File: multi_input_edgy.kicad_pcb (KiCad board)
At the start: 2 copper layers, 60 x 43.2 mm, 84 parts, among them J1 002, J2 002, J3 In1, J4 In2, J5 In3, J6 In4, J7 6V-24V, Q1 PMV213SN, Q10 DMP610DL, Q11 2N7002, Q12 2N7002, Q13 PMV213SN, Q14 DMP610DL, Q15 2N7002, Q16 2N7002, Q2 DMP610DL, Q3 2N7002, Q4 2N7002, Q5 PMV213SN, Q6 DMP610DL, Q7 2N7002, Q8 2N7002, Q9 PMV213SN, U1 EL3H7, U10 AL5809-15P, U11 EL3H7, U12 EL3H7, U13 AL5809-15P, U14 AL5809-15P, U15 EL3H7, U16 EL3H7, U17 HEF4021BT, U18 SN74LVC1G125, U2 AL5809-15P, U3 AL5809-15P, U4 EL3H7, U5 AL5809-15P, U6 AL5809-15P, U7 EL3H7, U8 EL3H7, U9 AL5809-15P

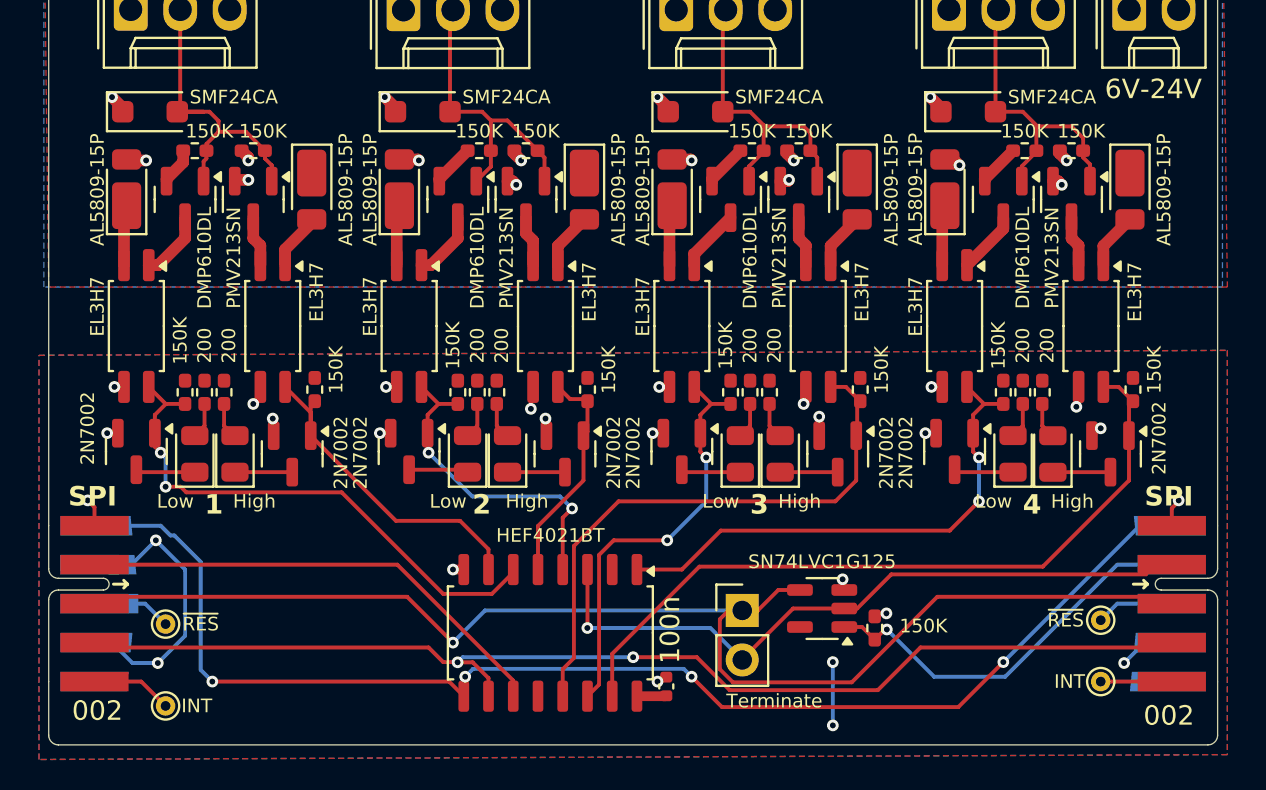
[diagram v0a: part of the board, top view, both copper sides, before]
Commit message: Fix constant current source (AL5809) symbol and footprint
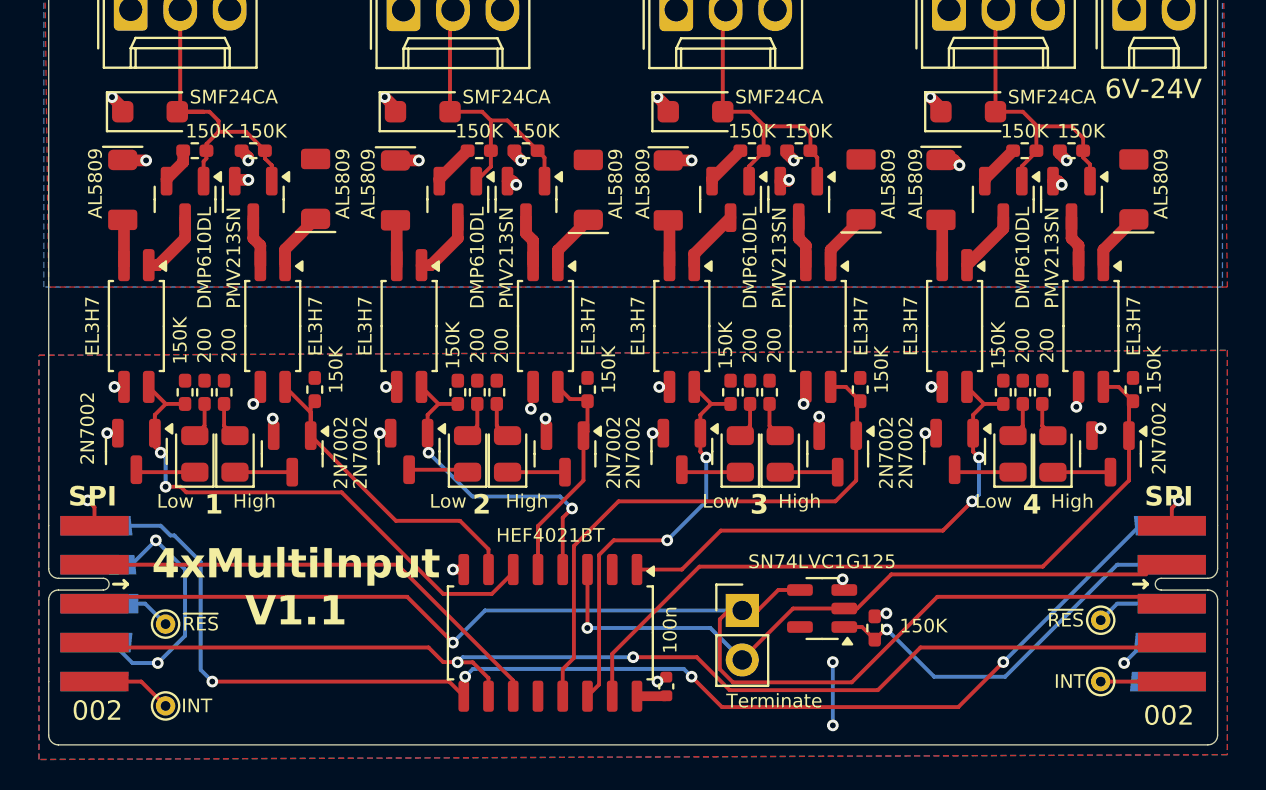
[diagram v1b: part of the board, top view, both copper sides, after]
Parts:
- U1, U11, U12, U15, U16, U4, U7, U8: footprint Package_SO:SSOP-4_4.4x2.6mm_P1.27mm -> lcsc_stuff:SSOP-4_4.4x2.6mm_P1.27mm
- U10, U13, U14, U2, U3, U5, U6, U9: value AL5809-15P -> AL5809; footprint Diode_SMD:D_PowerDI-123 -> lcsc_stuff:PowerDI-123
- moved U9 37.6 mm to (136.9, 50.4), turned to 90 degrees
- moved U6 37.6 mm to (188.6, 48.6), turned to -90 degrees
- moved U13 23.6 mm to (164.9, 50.4), turned to 90 degrees
- moved U3 23.6 mm to (160.6, 48.6), turned to -90 degrees
- moved U10 14.1 mm to (150.9, 50.4)
- moved U5 14.1 mm to (174.6, 48.6)
- moved U14 0.93 mm to (178.9, 50.4)
- moved U2 0.93 mm to (146.6, 48.6)
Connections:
- U10 pad 1: Net-(U10-VA) -> Net-(U10-in)
- U12 pad 2: Net-(U10-VA) -> Net-(U12-K)
- U13 pad 1: VDDA -> Net-(U12-K)
- U13 pad 2: Net-(U13-VB) -> GNDA
- U15 pad 1: Net-(U13-VB) -> Net-(U15-A)
- U3 pad 1: Net-(U3-VA) -> VDDA
- U3 pad 2: GNDA -> Net-(U3-Out)
- U4 pad 2: Net-(U3-VA) -> Net-(U4-K)
- U5 pad 2: Net-(U5-VB) -> Net-(U11-A)
- U6 pad 1: Net-(U6-VA) -> VDDA
- U6 pad 2: GNDA -> Net-(U15-A)
- U7 pad 1: Net-(U5-VB) -> Net-(U3-Out)
- U8 pad 2: Net-(U6-VA) -> Net-(U10-in)
- U9 pad 1: VDDA -> Net-(U4-K)
- U9 pad 2: Net-(U11-A) -> GNDA
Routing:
- net Net-(U6-VA): track 3.11 -> 0.00 mm
- net Net-(U3-VA): track 3.11 -> 0.00 mm
- net Net-(U10-VA): track 3.11 -> 0.00 mm
- net Net-(U15-A): track 0.00 -> 3.00 mm
- net Net-(U3-Out): track 0.00 -> 2.97 mm
- net Net-(U5-VB): track 2.92 -> 0.00 mm
- net Net-(U13-VB): track 2.92 -> 0.00 mm
- net Net-(U4-K): track 0.00 -> 2.35 mm
- net Net-(U10-in): track 0.00 -> 2.33 mm
- net Net-(U12-K): track 0.00 -> 2.31 mm
- net GNDA: track 12.8 -> 13.8 mm
- net Net-(U14-in): track 3.11 -> 2.35 mm
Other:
- board text added: "4xMultiInput V1.1"

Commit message: Get board name and version from text variable
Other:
- board text added: "${BoardName} ${Version}"
- board text removed: "4xMultiInput V1.1"
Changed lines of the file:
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@@
 		)
 	)
+	(property "BoardName" "4xMultiInput")
+	(property "Version" "V1.1")
 	(net 0 "")
 	(net 1 "GNDA")
@@
 	(net 15 "Net-(D9-K)")
 	(net 16 "Net-(D9-A)")
-	(net 17 "Net-(D11-A)")
-	(net 18 "Net-(D11-K)")
-	(net 19 "Net-(D12-A)")
-	(net 20 "Net-(D12-K)")
+	(net 17 "Net-(U14-in)")
+	(net 18 "Net-(U15-A)")
+	(net 19 "Net-(Q14-D)")
+	(net 20 "Net-(Q13-D)")
 	(net 21 "/4xInput/~{CS}")
 	(net 22 "/4xInput/MOSI")
@@
 	(net 27 "Net-(Q9-D)")
 	(net 28 "Net-(Q10-D)")
-	(net 29 "Net-(Q13-D)")
-	(net 30 "Net-(Q14-D)")
+	(net 29 "Net-(D12-K)")
+	(net 30 "Net-(D12-A)")
 	(net 31 "Net-(Q2-D)")
 	(net 32 "Net-(U1-A)")
@@
 	(net 34 "Net-(U11-A)")
 	(net 35 "Net-(U12-K)")
-	(net 36 "Net-(U15-A)")
+	(net 36 "Net-(D11-K)")
 	(net 37 "unconnected-(U17-Q6-Pad12)")
 	(net 38 "unconnected-(U17-Q5-Pad2)")
@@
 	(net 60 "Net-(U3-Out)")
 	(net 61 "Net-(U10-in)")
-	(net 62 "Net-(U14-in)")
+	(net 62 "Net-(D11-A)")
 	(footprint "Diode_SMD:D_SOD-123F"
 		(layer "F.Cu")
@@
 			(layers "F.Cu" "F.Mask" "F.Paste")
 			(roundrect_rratio 0.25)
-			(net 20 "Net-(D12-K)")
+			(net 29 "Net-(D12-K)")
 			(pinfunction "D")
 			(pintype "passive")
@@
 			(layers "F.Cu" "F.Mask" "F.Paste")
 			(roundrect_rratio 0.25)
-			(net 29 "Net-(Q13-D)")
+			(net 20 "Net-(Q13-D)")
 			(pinfunction "D")
 			(pintype "passive")
@@
 			(layers "F.Cu" "F.Mask" "F.Paste")
 			(roundrect_rratio 0.25)
-			(net 36 "Net-(U15-A)")
+			(net 18 "Net-(U15-A)")
 			(pinfunction "A")
 			(pintype "passive")
@@
 			(layers "F.Cu" "F.Mask" "F.Paste")
 			(roundrect_rratio 0.25)
-			(net 29 "Net-(Q13-D)")
+			(net 20 "Net-(Q13-D)")
 			(pinfunction "K")
 			(pintype "passive")
@@
 		)
 		(fp_text user "${REFERENCE}"
-			(at 0 2.5 270)
+			(at 0 2.5 -90)
 			(unlocked yes)
 			(layer "F.SilkS")
@@
 			(layers "F.Cu" "F.Mask" "F.Paste")
 			(roundrect_rratio 0.25)
-			(net 20 "Net-(D12-K)")
+			(net 29 "Net-(D12-K)")
 			(pinfunction "K")
 			(pintype "passive")
@@
 			(layers "F.Cu" "F.Mask" "F.Paste")
 			(roundrect_rratio 0.25)
-			(net 19 "Net-(D12-A)")
+			(net 30 "Net-(D12-A)")
 			(pinfunction "A")
 			(pintype "passive")
@@
 			(layers "F.Cu" "F.Mask" "F.Paste")
 			(roundrect_rratio 0.25)
-			(net 30 "Net-(Q14-D)")
+			(net 19 "Net-(Q14-D)")
 			(pinfunction "A")
 			(pintype "passive")
@@
 			(layers "F.Cu" "F.Mask" "F.Paste")
 			(roundrect_rratio 0.25)
-			(net 62 "Net-(U14-in)")
+			(net 17 "Net-(U14-in)")
 			(pinfunction "K")
 			(pintype "passive")
@@
 			(layers "F.Cu" "F.Mask" "F.Paste")
 			(roundrect_rratio 0.25)
-			(net 19 "Net-(D12-A)")
+			(net 30 "Net-(D12-A)")
 			(pintype "passive")
 		)
@@
 		)
 		(fp_text user "${REFERENCE}"
-			(at 0 2.5 270)
+			(at 0 2.5 -90)
 			(unlocked yes)
 			(layer "F.SilkS")
@@
 			(layers "F.Cu" "F.Mask" "F.Paste")
 			(roundrect_rratio 0.2380952381)
-			(net 36 "Net-(U15-A)")
+			(net 18 "Net-(U15-A)")
 			(pinfunction "Out")
 			(pintype "input")
@@
 		)
 		(fp_text user "${REFERENCE}"
-			(at 0 2.5 270)
+			(at 0 2.5 -90)
 			(unlocked yes)
 			(layer "F.SilkS")
@@
 			(layers "F.Cu" "F.Mask" "F.Paste")
 			(roundrect_rratio 0.25)
-			(net 30 "Net-(Q14-D)")
+			(net 19 "Net-(Q14-D)")
 			(pinfunction "D")
 			(pintype "passive")
@@
 			(layers "F.Cu" "F.Mask" "F.Paste")
 			(roundrect_rratio 0.25)
-			(net 18 "Net-(D11-K)")
+			(net 36 "Net-(D11-K)")
 			(pinfunction "K")
 			(pintype "passive")
@@
 			(layers "F.Cu" "F.Mask" "F.Paste")
 			(roundrect_rratio 0.25)
-			(net 17 "Net-(D11-A)")
+			(net 62 "Net-(D11-A)")
 			(pinfunction "A")
 			(pintype "passive")
@@
 			(layers "F.Cu" "F.Mask" "F.Paste")
 			(roundrect_rratio 0.1666666667)
-			(net 62 "Net-(U14-in)")
+			(net 17 "Net-(U14-in)")
 			(pinfunction "in")
 			(pintype "input")
@@
 			(layers "F.Cu" "F.Mask" "F.Paste")
 			(roundrect_rratio 0.25)
-			(net 17 "Net-(D11-A)")
+			(net 62 "Net-(D11-A)")
 			(pintype "passive")
 		)
@@
 			(layers "F.Cu" "F.Mask" "F.Paste")
 			(roundrect_rratio 0.25)
-			(net 18 "Net-(D11-K)")
+			(net 36 "Net-(D11-K)")
 			(pinfunction "D")
 			(pintype "passive")
@@
 		(layer "Edge.Cuts")
 	)
+	(gr_text "${BoardName}\n${Version}\n"
+		(at 145.6 72.2 0)
+		(layer "F.SilkS")
+		(effects
+			(font
+				(size 1.5 1.5)
+				(thickness 0.3)
+				(bold yes)
+			)
+			(justify bottom)
+		)
+	)
 	(gr_text "1"
 		(at 141 66.25 0)
@@
 		)
 	)
-	(gr_text "4xMultiInput\nV1.1"
-		(at 145.7 72 0)
-		(layer "F.SilkS")
-		(effects
-			(font
-				(size 1.5 1.5)
-				(thickness 0.3)
-				(bold yes)
-			)
-			(justify bottom)
-		)
-	)
 	(gr_text "+"
 		(at 169.71 37.1 0)
@@
 	)
 	(segment
-		(start 184 60.5)
-		(end 184 61.625)
-		(width 0.2)
+		(start 178.865 51.115)
+		(end 178.8 51.05)
+		(width 0.6)
 		(layer "F.Cu")
 		(net 17)
 	)
 	(segment
-		(start 184 61.625)
-		(end 184.5 62.125)
-		(width 0.2)
+		(start 178.865 53.375)
+		(end 178.865 51.115)
+		(width 0.6)
 		(layer "F.Cu")
 		(net 17)
 	)
 	(segment
-		(start 184.5 64)
-		(end 187.5 64)
-		(width 0.2)
+		(start 187.135 52.59)
+		(end 188.7 51.025)
+		(width 0.6)
 		(layer "F.Cu")
 		(net 18)
 	)
 	(segment
-		(start 183 60.5)
-		(end 183 61.625)
-		(width 0.2)
+		(start 187.135 53.375)
+		(end 187.135 52.59)
+		(width 0.6)
+		(layer "F.Cu")
+		(net 18)
+	)
+	(segment
+		(start 180.135 53.375)
+		(end 182 51.51)
+		(width 0.6)
 		(layer "F.Cu")
 		(net 19)
 	)
 	(segment
-		(start 183 61.625)
-		(end 182.5 62.125)
-		(width 0.2)
+		(start 182 51.51)
+		(end 182 50.9375)
+		(width 0.6)
 		(layer "F.Cu")
 		(net 19)
 	)
 	(segment
-		(start 179.625 64)
-		(end 179.5 63.875)
-		(width 0.2)
+		(start 185.865 53.375)
+		(end 185.865 52.365)
+		(width 0.6)
 		(layer "F.Cu")
 		(net 20)
 	)
 	(segment
-		(start 182.5 64)
-		(end 179.625 64)
-		(width 0.2)
+		(start 185.865 52.365)
+		(end 185.5 52)
+		(width 0.6)
+		(layer "F.Cu")
+		(net 20)
+	)
+	(segment
+		(start 185.5 52)
+		(end 185.5 50.9375)
+		(width 0.6)
 		(layer "F.Cu")
 		(net 20)
@@
 	)
 	(segment
-		(start 185.865 53.375)
-		(end 185.865 52.365)
-		(width 0.6)
-		(layer "F.Cu")
-		(net 29)
-	)
-	(segment
-		(start 185.865 52.365)
-		(end 185.5 52)
-		(width 0.6)
+		(start 179.625 64)
+		(end 179.5 63.875)
+		(width 0.2)
 		(layer "F.Cu")
 		(net 29)
 	)
 	(segment
-		(start 185.5 52)
-		(end 185.5 50.9375)
-		(width 0.6)
+		(start 182.5 64)
+		(end 179.625 64)
+		(width 0.2)
 		(layer "F.Cu")
 		(net 29)
 	)
 	(segment
-		(start 180.135 53.375)
-		(end 182 51.51)
-		(width 0.6)
+		(start 183 60.5)
+		(end 183 61.625)
+		(width 0.2)
 		(layer "F.Cu")
 		(net 30)
 	)
 	(segment
-		(start 182 51.51)
-		(end 182 50.9375)
-		(width 0.6)
+		(start 183 61.625)
+		(end 182.5 62.125)
+		(width 0.2)
 		(layer "F.Cu")
 		(net 30)
@@
 	)
 	(segment
-		(start 187.135 52.59)
-		(end 188.7 51.025)
-		(width 0.6)
-		(layer "F.Cu")
-		(net 36)
-	)
-	(segment
-		(start 187.135 53.375)
-		(end 187.135 52.59)
-		(width 0.6)
+		(start 184.5 64)
+		(end 187.5 64)
+		(width 0.2)
 		(layer "F.Cu")
 		(net 36)
@@
 	)
 	(segment
-		(start 178.865 51.115)
-		(end 178.8 51.05)
-		(width 0.6)
+		(start 184 60.5)
+		(end 184 61.625)
+		(width 0.2)
 		(layer "F.Cu")
 		(net 62)
 	)
 	(segment
-		(start 178.865 53.375)
-		(end 178.865 51.115)
-		(width 0.6)
+		(start 184 61.625)
+		(end 184.5 62.125)
+		(width 0.2)
 		(layer "F.Cu")
 		(net 62)
